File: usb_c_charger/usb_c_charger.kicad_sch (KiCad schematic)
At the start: 0 parts

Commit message: Updated Schematic - USB Wiring / dual Battery Connectors / Decoupling Capacitors / Status LED
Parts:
- added C1: 1u, symbol Device:C_Small
- added C2: 20u, symbol Device:C_Small
- added C3, C5: 10u, symbol Device:C_Small
- added C4: 47n, symbol Device:C_Small
- added C6: 4.7u, symbol Device:C_Small
- added D1: LED, symbol Device:LED
- added J1: USB_C_Receptacle_USB2.0_16P, symbol Connector:USB_C_Receptacle_USB2.0_16P
- added J2: JST_LiPo, symbol Connector_Generic:Conn_01x02
- added J3: 18650_Holder, symbol Connector_Generic:Conn_01x02
- added L1: 1u, symbol Device:L
- added R1, R2: 5.1k, symbol Device:R
- added R3: 226, symbol Device:R
- added R4: 160, symbol Device:R
- added R5: 10k, symbol Device:R
- added R6: 1k, symbol Device:R
- added SW1: SW_SPDT, symbol Switch:SW_SPDT
- added U1: BQ25606RGER, BQ25606RGER:QFN50P400X400X100-25N, symbol BQ25606RGER:BQ25606RGER
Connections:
- new net: J1.A5 (CC1), R1.1
- new net: J1.B5 (CC2), R2.1
- new net: R4.2, U1.8 (ILIM)
- new net: J2.1 (Pin_1), SW1.1 (A)
- new net: J3.1 (Pin_1), SW1.3 (C)
- new net: C4.2, U1.21 (BTST)
- new net: R5.2, U1.11 (TS)
- new net: D1.1 (K), U1.5 (STAT)
- new net: D1.2 (A), R6.2
- new net: C6.2, U1.22 (REGN)
- new net: R3.2, U1.10 (ICHG)
- new net: C5.2, U1.23 (PMID)
- new net BAT: C3.1, SW1.2 (B), U1.13 (BAT-1), U1.14 (BAT)
- new net D+: J1.A6 (D+), J1.B6 (D+), U1.3 (D+)
- new net D-: J1.A7 (D-), J1.B7 (D-), U1.4 (D-)
- new net GND: C1.2, C2.2, C3.2, C5.1, C6.1, J1.A1 (GND), J1.A12 (GND), J1.B1 (GND), J1.B12 (GND), J2.2 (Pin_2), J3.2 (Pin_2), R1.2, R2.2, R3.1, R4.1, R5.1, U1.17 (GND-1), U1.18 (GND), U1.9 (~{CE})
- new net SW: C4.1, L1.2, U1.19 (SW-1), U1.20 (SW)
- new net SYS_PWR: C2.1, L1.1, U1.15 (SYS-1), U1.16 (SYS)
- new net VBUS: C1.1, J1.A4 (VBUS), J1.A9 (VBUS), J1.B4 (VBUS), J1.B9 (VBUS), R6.1, U1.1 (VAC), U1.24 (VBUS)
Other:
- title: (none) -> USB-C Dual Battery Charger

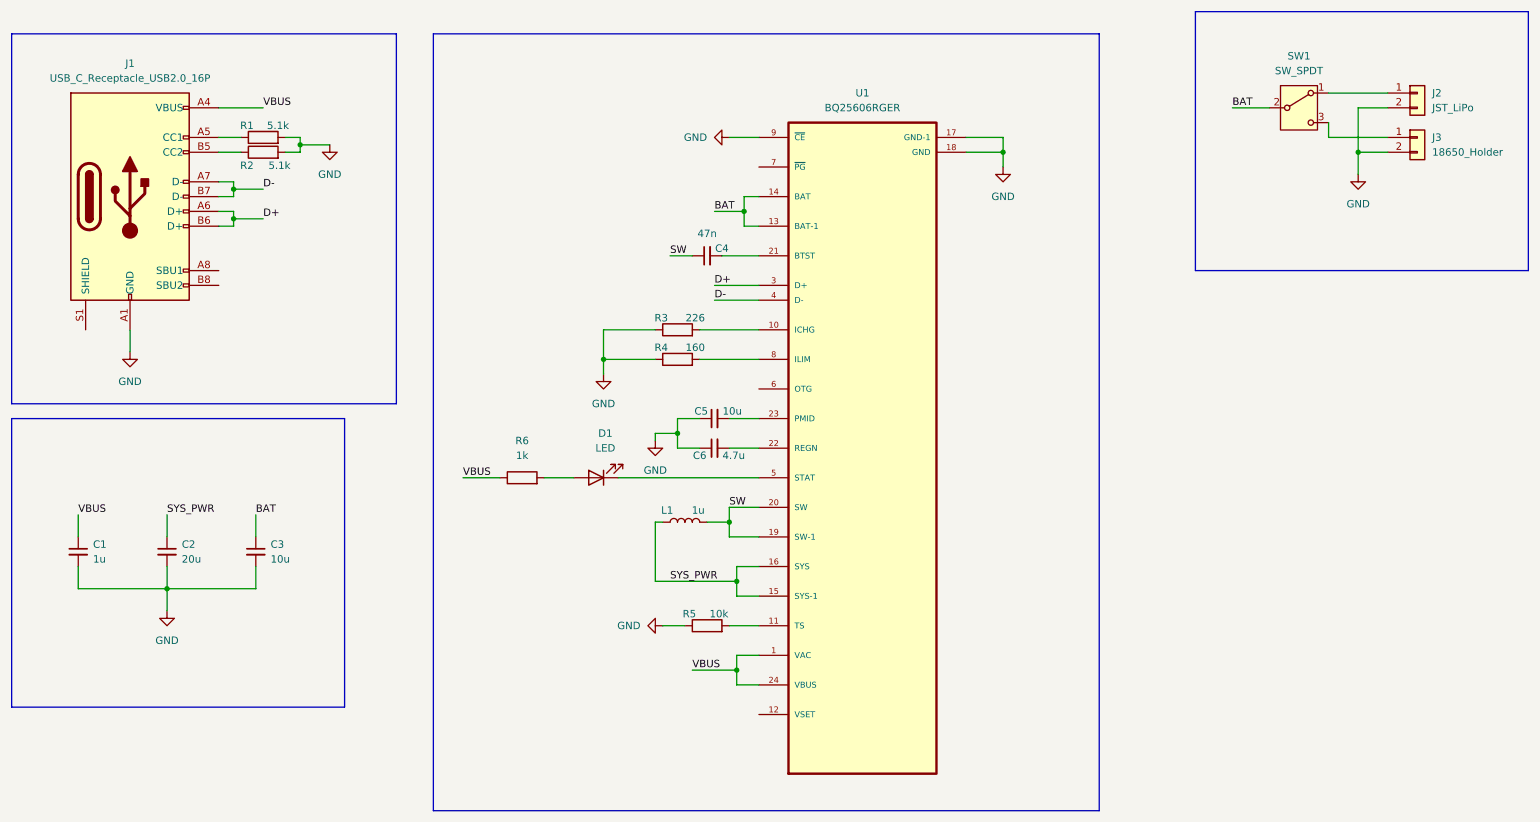
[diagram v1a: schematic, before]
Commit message: Finished Schematic Routing and PCB Components Initial Placements
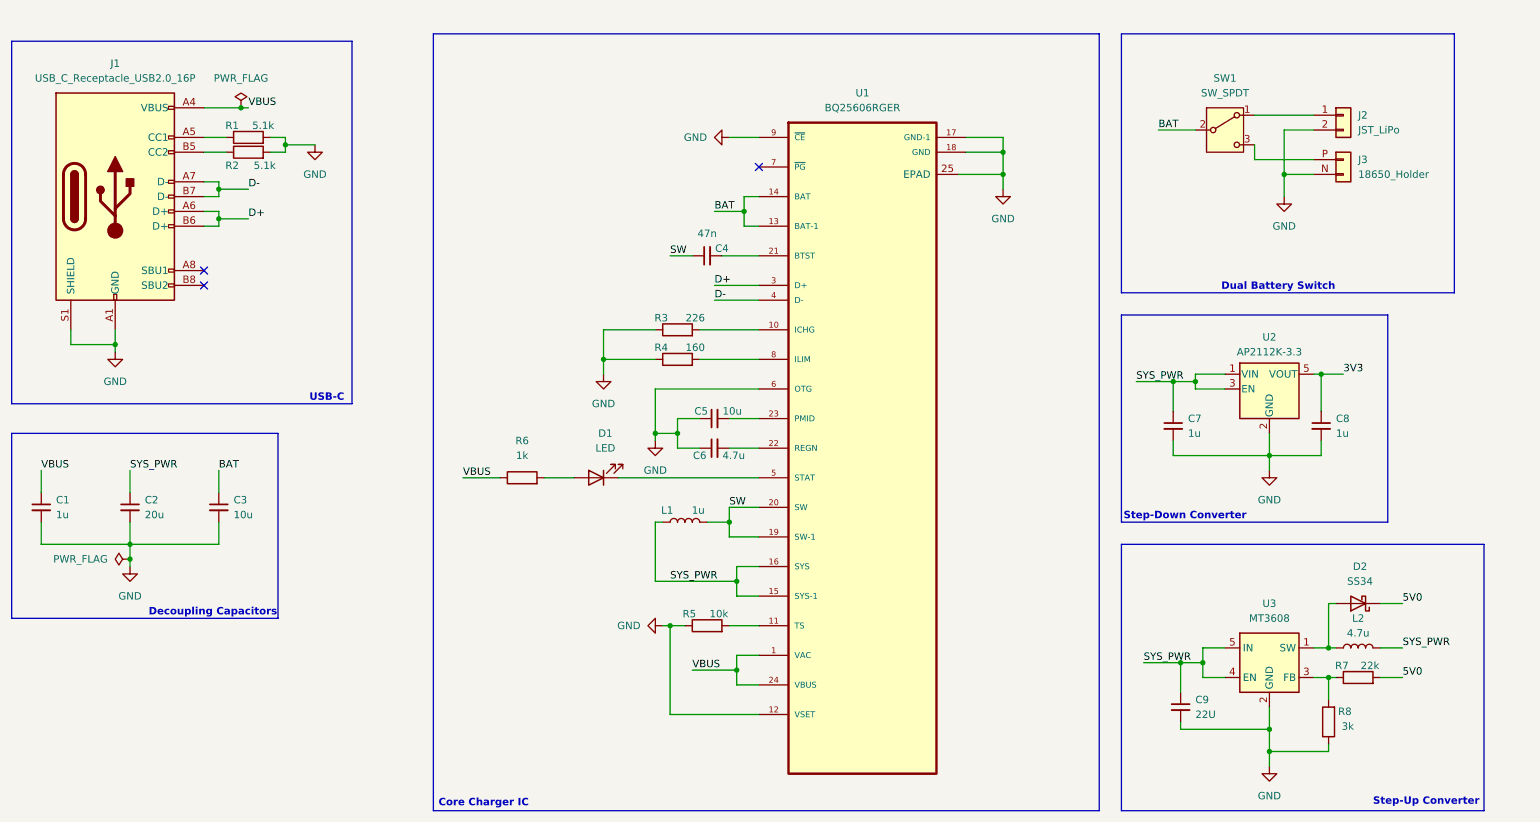
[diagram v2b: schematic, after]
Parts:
- added C7, C8: 1u, Capacitor_SMD:C_0805_2012Metric, symbol Device:C_Small
- added C9: 22U, Capacitor_SMD:C_1206_3216Metric, symbol Device:C_Small
- added D2: SS34, Diode_SMD:D_SMA, symbol Diode:SS34
- added L2: 4.7u, Inductor_SMD:L_6.3x6.3_H3, symbol Device:L
- added R7: 22k, Resistor_SMD:R_0805_2012Metric, symbol Device:R
- added R8: 3k, Resistor_SMD:R_0805_2012Metric, symbol Device:R
- added U2: AP2112K-3.3, Package_TO_SOT_SMD:SOT-23-5, symbol Regulator_Linear:AP2112K-3.3
- added U3: MT3608, Package_TO_SOT_SMD:SOT-23-6, symbol Regulator_Switching:MT3608
- C1, C3, C4, C5, C6: footprint (none) -> Capacitor_SMD:C_0805_2012Metric
- C2: footprint (none) -> Capacitor_SMD:C_1206_3216Metric
- D1: footprint (none) -> LED_SMD:LED_0805_2012Metric
- J1: footprint (none) -> Connector_USB:USB_C_Receptacle_HRO_TYPE-C-31-M-12
- J2: footprint (none) -> Connector_JST:JST_PH_S2B-PH-K_1x02_P2.00mm_Horizontal
- J3: footprint (none) -> 1043:BAT_1043
- L1: footprint (none) -> Inductor_SMD:L_6.3x6.3_H3
- R1, R2, R3, R4, R5, R6: footprint (none) -> Resistor_SMD:R_0805_2012Metric
- SW1: footprint (none) -> EG1218:SW_EG1218
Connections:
- net GND: now also J1.S1 (SHIELD), J3.N (Pin_2), U1.12 (VSET), U1.25 (EPAD), U1.6 (OTG), C7.2, C8.2, C9.2, R8.1, U2.2 (GND), U3.2 (GND); no longer J3.2 (Pin_2)
- net SYS_PWR: now also C7.1, C9.1, L2.2, U2.1 (VIN), U2.3 (EN), U3.4 (EN), U3.5 (IN)
- net at SW1.3 (C): now also J3.P (Pin_1); no longer J3.1 (Pin_1)
- new net: D2.2 (A), L2.1, U3.1 (SW)
- new net: R7.1, R8.2, U3.3 (FB)
- new net 3V3: C8.1, U2.5 (VOUT)
- new net 5V0: D2.1 (K), R7.2
- no-connect marks 0 -> 3
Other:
- note added: "Core Charger IC"
- note added: "Decoupling Capacitors"
- note added: "Dual Battery Switch"
- note added: "Step-Down Converter"
- note added: "Step-Up Converter"
- note added: "USB-C"
- moved on the sheet: C1, C2, C3, J1, J2, J3, R1, R2, SW1
